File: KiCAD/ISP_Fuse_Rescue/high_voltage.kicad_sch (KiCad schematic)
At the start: 11 parts, among them U3 MC34063AP

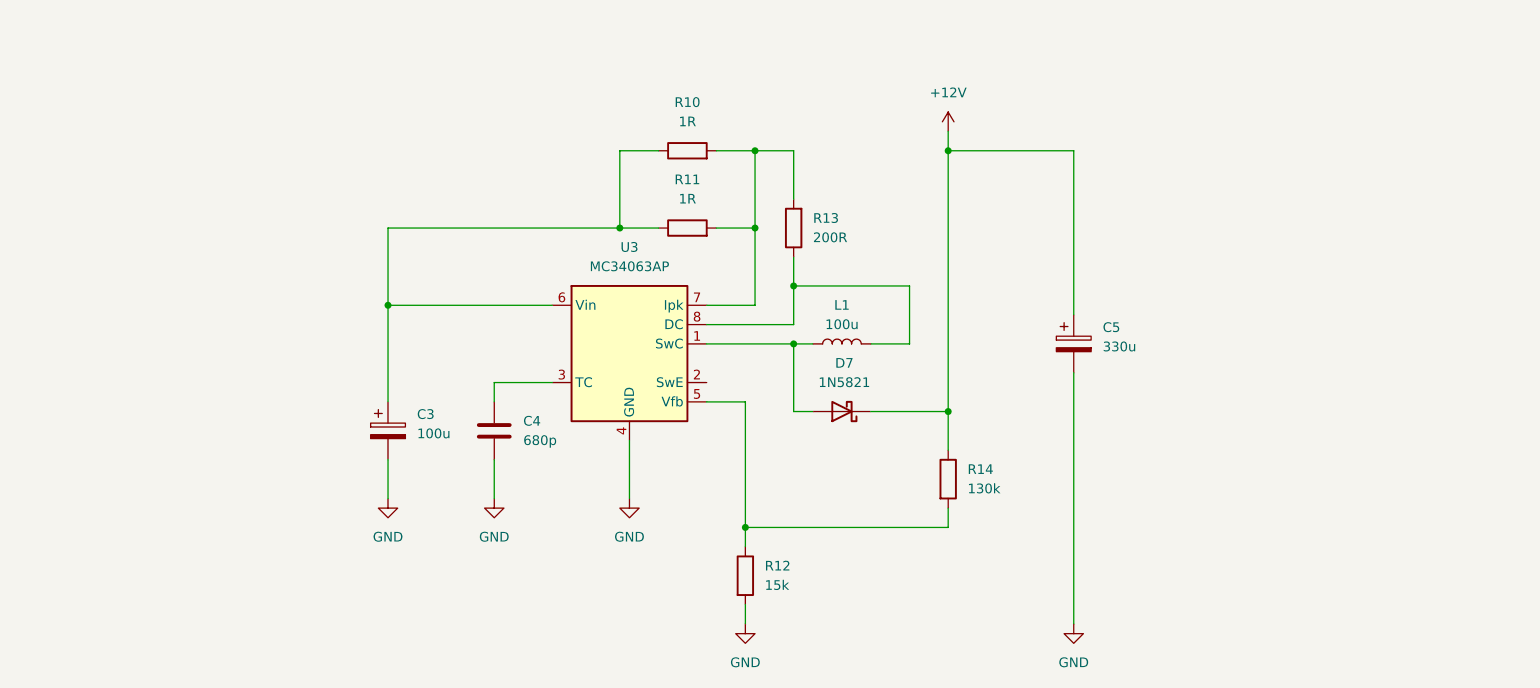
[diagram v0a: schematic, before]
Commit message: ISP Fuse Rescue
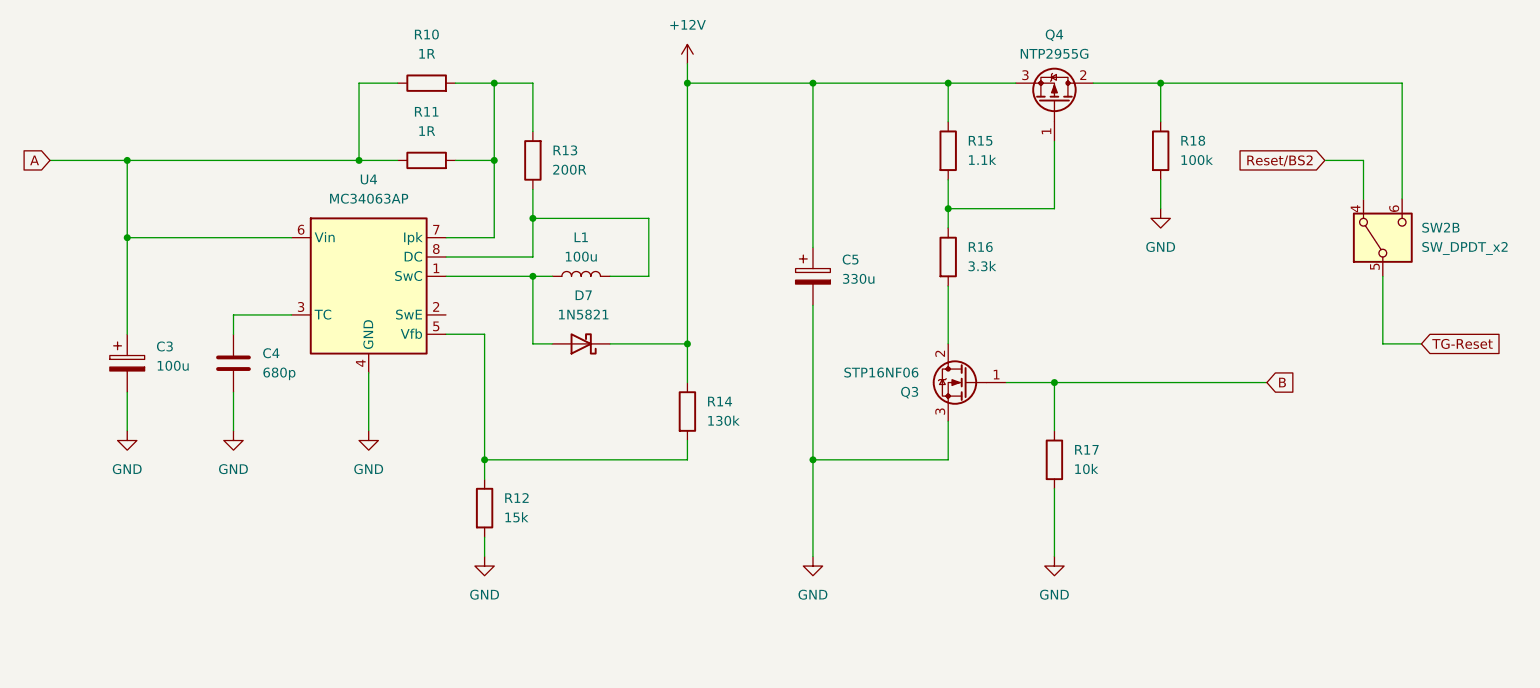
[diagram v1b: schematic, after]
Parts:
- added Q3: STP16NF06, My_Misc:TO-220-3_Vertical_larger, symbol My_Misc:STP16NF06
- added Q4: NTP2955G, My_Misc:TO-220-3_Vertical_larger, symbol My_Misc:NTP2955G
- added R15: 1.1k, My_Misc:R_Axial_DIN0207_L6.3mm_D2.5mm_P10.16mm_Horizontal_large, symbol Device:R
- added R16: 3.3k, My_Misc:R_Axial_DIN0207_L6.3mm_D2.5mm_P10.16mm_Horizontal_large, symbol Device:R
- added R17: 10k, My_Misc:R_Axial_DIN0207_L6.3mm_D2.5mm_P10.16mm_Horizontal_large, symbol Device:R
- added R18: 100k, My_Misc:R_Axial_DIN0207_L6.3mm_D2.5mm_P10.16mm_Horizontal_large, symbol Device:R
- added SW2: SW_DPDT_x2, My_Parts:Switch sub-miniatyr 2-pole on-on, symbol Switch:SW_DPDT_x2
- C3, C5: footprint (none) -> My_Misc:CP_Radial_D5.0mm_P2.50mm_larger_pads
- C4: footprint (none) -> My_Misc:C_Disc_D3.0mm_W1.6mm_P2.50mm_larg
- L1: footprint (none) -> My_Misc:L_Radial_D8.7mm_P5.00mm_Fastron_07HCP
- R10, R11, R12, R13, R14: footprint (none) -> My_Misc:R_Axial_DIN0207_L6.3mm_D2.5mm_P10.16mm_Horizontal_large
- U4: renamed from U3; footprint Package_DIP:DIP-8_W7.62mm -> My_Misc:DIP-8_W7.62mm_Socket_w_dip_packet_LongPads
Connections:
- net +12V: now also Q4.3 (S), R15.1
- net GND: now also Q3.3 (S), R17.2, R18.2
- net A: now reaches C3.1, R10.1, R11.1, U4.6 (Vin)
- new net: Q4.2 (D), R18.1, SW2.6 (C)
- new net: Q4.1 (G), R15.2, R16.1
- new net: Q3.2 (D), R16.2
- new net B: Q3.1 (G), R17.1
- new net Reset/BS2: SW2.4 (A)
- new net TG-Reset: SW2.5 (B)
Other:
- moved on the sheet: C3, C4, C5, D7, L1, R10, R11, R12, R13, R14, U4
